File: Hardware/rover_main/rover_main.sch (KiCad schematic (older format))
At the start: 32 parts, among them J1 BATT, J10 Analog, J2 BME280, J3 CSS811, J4 DRIVERS, J5 GY-87, J6 PROG, J7 FTDI, J8 Digital, J9 i2c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

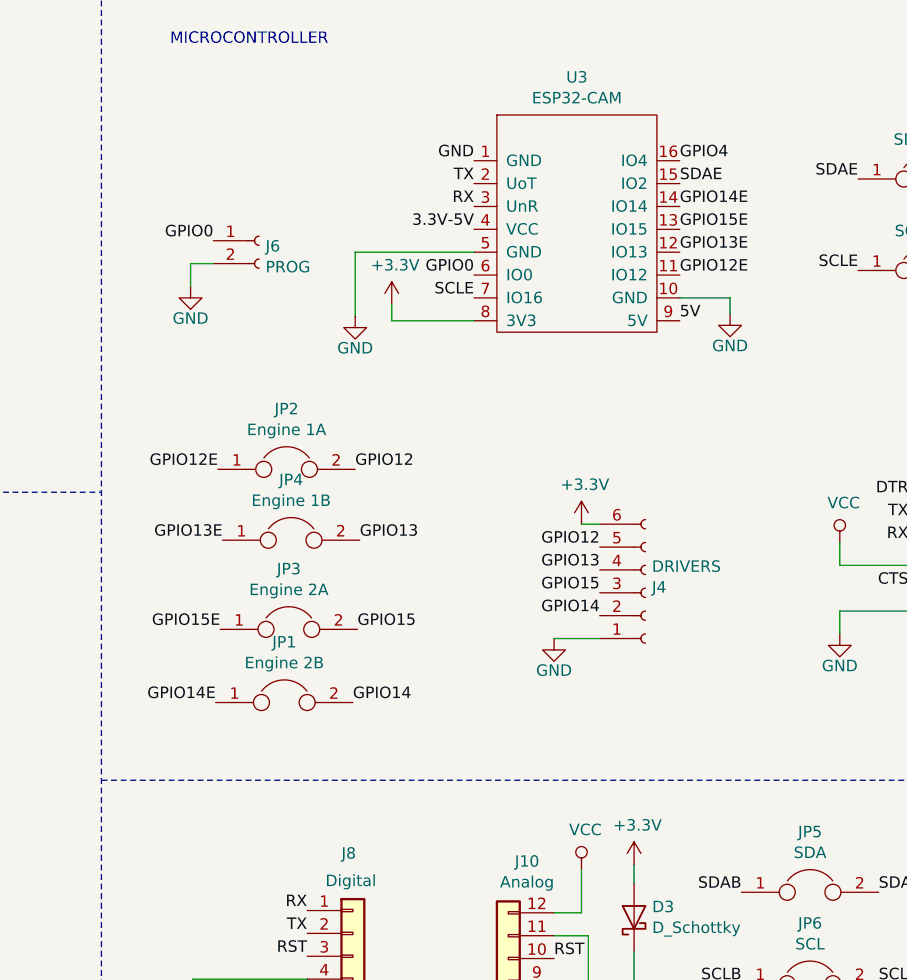
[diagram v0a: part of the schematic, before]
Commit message: Add SDA to jumper
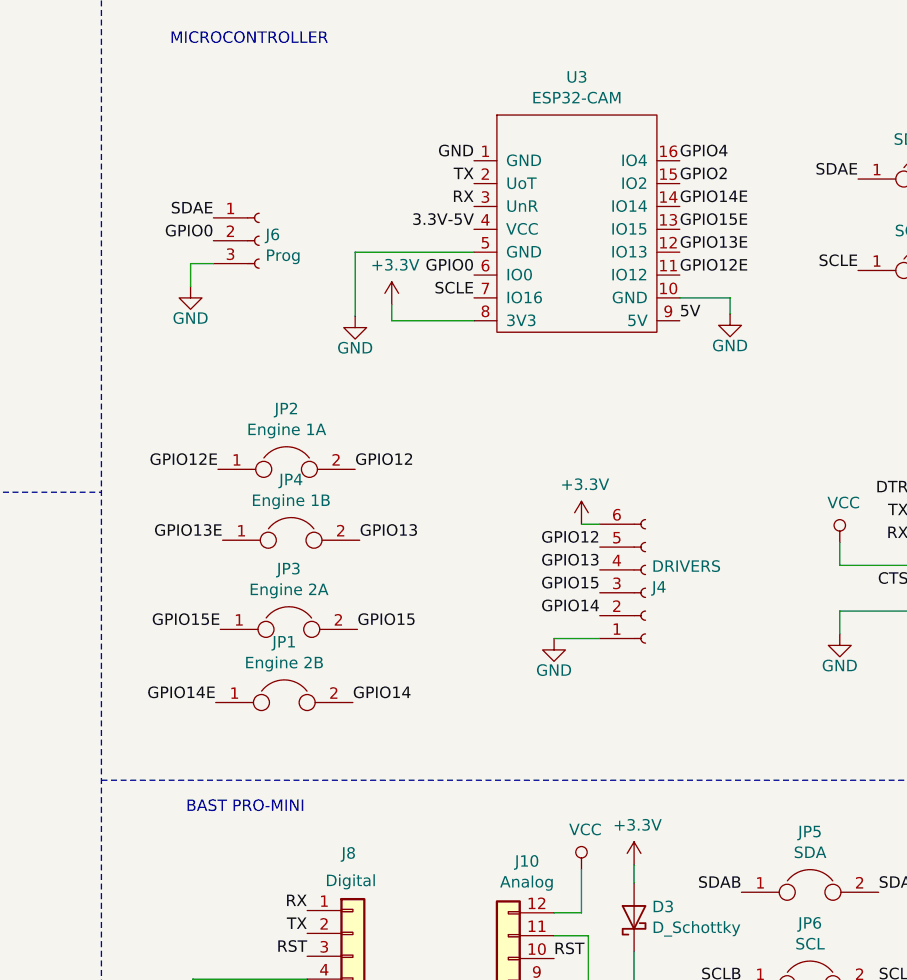
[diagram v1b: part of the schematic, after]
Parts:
- removed J6: PROG, Connector_PinSocket_2.54mm:PinSocket_1x02_P2.54mm_Vertical, symbol Connector:Conn_01x02_Female
- added J6: Prog, Connector_PinHeader_2.54mm:PinHeader_1x03_P2.54mm_Vertical, symbol Connector:Conn_01x03_Female
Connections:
- net GND: now also J6.3 (Pin_3)
- net GPIO0: now also J6.2 (Pin_2)
- net SDAE: now also J6.1 (Pin_1); no longer U3.15 (IO2)
- new net GPIO2: U3.15 (IO2)
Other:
- note added: "BAST PRO-MINI\n"
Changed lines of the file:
@@
 Text Label 10310 1280 2    50   ~ 0
 SDAE
-Text Label 9530 1300 0    50   ~ 0
+Text Label 7490 1450 2    50   ~ 0
 SDAE
 $Comp
@@
 9
 $Comp
-L Connector:Conn_01x02_Female J6
-U 1 1 5D5E84D2
-P 7690 1550
-F 0 "J6" H 7718 1526 50  0000 L CNN
-F 1 "PROG" H 7718 1435 50  0000 L CNN
-F 2 "Connector_PinSocket_2.54mm:PinSocket_1x02_P2.54mm_Vertical" H 7690 1550 50  0001 C CNN
-F 3 "~" H 7690 1550 50  0001 C CNN
-	1    7690 1550
-	1    0    0    -1
-$EndComp
-$Comp
 L Connector:Conn_01x06_Female J2
 U 1 1 5D49D204
@@
 Wire Wire Line
 	9330 4660 9330 4790
+$Comp
+L Connector:Conn_01x03_Female J6
+U 1 1 5D4B08DF
+P 7690 1550
+F 0 "J6" H 7718 1576 50  0000 L CNN
+F 1 "Prog" H 7718 1485 50  0000 L CNN
+F 2 "Connector_PinHeader_2.54mm:PinHeader_1x03_P2.54mm_Vertical" H 7690 1550 50  0001 C CNN
+F 3 "~" H 7690 1550 50  0001 C CNN
+	1    7690 1550
+	1    0    0    -1
+$EndComp
+Text Label 9530 1300 0    50   ~ 0
+GPIO2
+Text Notes 7370 4060 0    50   ~ 0
+BAST PRO-MINI\n
 $EndSCHEMATC

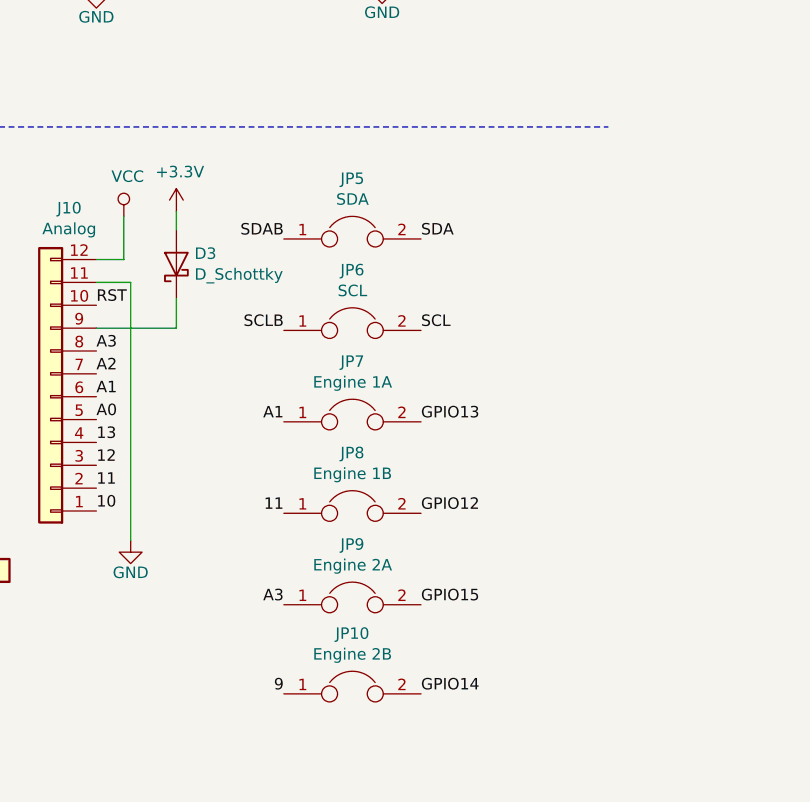
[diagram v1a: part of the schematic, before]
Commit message: change jumper open in sch
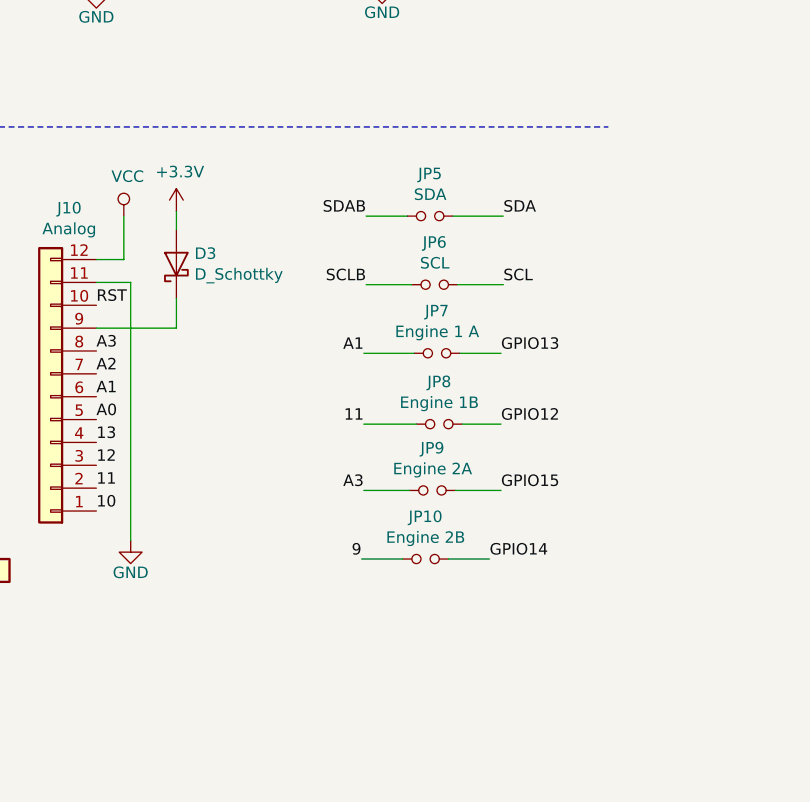
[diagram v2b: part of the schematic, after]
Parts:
- removed JP10: Engine 2B, Jumper:SolderJumper-2_P1.3mm_Open_RoundedPad1.0x1.5mm, symbol Device:Jumper
- removed JP5: SDA, Jumper:SolderJumper-2_P1.3mm_Open_RoundedPad1.0x1.5mm, symbol Device:Jumper
- removed JP6: SCL, Jumper:SolderJumper-2_P1.3mm_Open_RoundedPad1.0x1.5mm, symbol Device:Jumper
- removed JP7: Engine 1A, Jumper:SolderJumper-2_P1.3mm_Open_RoundedPad1.0x1.5mm, symbol Device:Jumper
- removed JP8: Engine 1B, Jumper:SolderJumper-2_P1.3mm_Open_RoundedPad1.0x1.5mm, symbol Device:Jumper
- removed JP9: Engine 2A, Jumper:SolderJumper-2_P1.3mm_Open_RoundedPad1.0x1.5mm, symbol Device:Jumper
- added JP10: Engine 2B, Jumper:SolderJumper-2_P1.3mm_Open_RoundedPad1.0x1.5mm, symbol Device:Jumper_NO_Small
- added JP5: SDA, Jumper:SolderJumper-2_P1.3mm_Open_RoundedPad1.0x1.5mm, symbol Device:Jumper_NO_Small
- added JP6: SCL, Jumper:SolderJumper-2_P1.3mm_Open_RoundedPad1.0x1.5mm, symbol Device:Jumper_NO_Small
- added JP7: Engine 1 A, Jumper:SolderJumper-2_P1.3mm_Open_RoundedPad1.0x1.5mm, symbol Device:Jumper_NO_Small
- added JP8: Engine 1B, Jumper:SolderJumper-2_P1.3mm_Open_RoundedPad1.0x1.5mm, symbol Device:Jumper_NO_Small
- added JP9: Engine 2A, Jumper:SolderJumper-2_P1.3mm_Open_RoundedPad1.0x1.5mm, symbol Device:Jumper_NO_Small
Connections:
- net 11: now also JP8.1
- net 9: now also JP10.1
- net A1: now also JP7.1
- net A3: now also JP9.1
- net GPIO12: now also JP8.2
- net GPIO13: now also JP7.2
- net GPIO14: now also JP10.2
- net GPIO15: now also JP9.2
- net SCL: now also JP6.2
- net SCLB: now also JP6.1
- net SDA: now also JP5.2
- net SDAB: now also JP5.1
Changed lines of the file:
@@
 	0    -1   -1   0
 $EndComp
-$Comp
-L Device:Jumper JP5
-U 1 1 5D4C2B76
-P 10100 4400
-F 0 "JP5" H 10100 4664 50  0000 C CNN
-F 1 "SDA" H 10100 4573 50  0000 C CNN
-F 2 "Jumper:SolderJumper-2_P1.3mm_Open_RoundedPad1.0x1.5mm" H 10100 4400 50  0001 C CNN
-F 3 "~" H 10100 4400 50  0001 C CNN
-	1    10100 4400
-	1    0    0    -1
-$EndComp
-$Comp
-L Device:Jumper JP6
-U 1 1 5D4C33A6
-P 10100 4800
-F 0 "JP6" H 10100 5064 50  0000 C CNN
-F 1 "SCL" H 10100 4973 50  0000 C CNN
-F 2 "Jumper:SolderJumper-2_P1.3mm_Open_RoundedPad1.0x1.5mm" H 10100 4800 50  0001 C CNN
-F 3 "~" H 10100 4800 50  0001 C CNN
-	1    10100 4800
-	1    0    0    -1
-$EndComp
-Text Label 10400 4800 0    50   ~ 0
+Text Label 10760 4600 0    50   ~ 0
 SCL
-Text Label 10400 4400 0    50   ~ 0
+Text Label 10760 4300 0    50   ~ 0
 SDA
-Text Label 9800 4400 2    50   ~ 0
+Text Label 10160 4300 2    50   ~ 0
 SDAB
 Text Label 8450 6050 3    50   ~ 0
 SDAB
-Text Label 9800 4800 2    50   ~ 0
+Text Label 10160 4600 2    50   ~ 0
 SCLB
 Text Label 8550 6050 3    50   ~ 0
 SCLB
-$Comp
-L Device:Jumper JP10
-U 1 1 5D4C8EC9
-P 10100 6390
-F 0 "JP10" H 10100 6654 50  0000 C CNN
-F 1 "Engine 2B" H 10100 6563 50  0000 C CNN
-F 2 "Jumper:SolderJumper-2_P1.3mm_Open_RoundedPad1.0x1.5mm" H 10100 6390 50  0001 C CNN
-F 3 "~" H 10100 6390 50  0001 C CNN
-	1    10100 6390
-	1    0    0    -1
-$EndComp
-$Comp
-L Device:Jumper JP9
-U 1 1 5D4C93D4
-P 10100 6000
-F 0 "JP9" H 10100 6264 50  0000 C CNN
-F 1 "Engine 2A" H 10100 6173 50  0000 C CNN
-F 2 "Jumper:SolderJumper-2_P1.3mm_Open_RoundedPad1.0x1.5mm" H 10100 6000 50  0001 C CNN
-F 3 "~" H 10100 6000 50  0001 C CNN
-	1    10100 6000
-	1    0    0    -1
-$EndComp
-$Comp
-L Device:Jumper JP8
-U 1 1 5D4C97D6
-P 10100 5600
-F 0 "JP8" H 10100 5864 50  0000 C CNN
-F 1 "Engine 1B" H 10100 5773 50  0000 C CNN
-F 2 "Jumper:SolderJumper-2_P1.3mm_Open_RoundedPad1.0x1.5mm" H 10100 5600 50  0001 C CNN
-F 3 "~" H 10100 5600 50  0001 C CNN
-	1    10100 5600
-	1    0    0    -1
-$EndComp
-Text Label 9800 6000 2    50   ~ 0
+Text Label 10150 5500 2    50   ~ 0
 A3
-Text Label 10400 5600 0    50   ~ 0
+Text Label 10750 5210 0    50   ~ 0
 GPIO12
-$Comp
-L Device:Jumper JP7
-U 1 1 5D4C892D
-P 10100 5200
-F 0 "JP7" H 10100 5464 50  0000 C CNN
-F 1 "Engine 1A" H 10100 5373 50  0000 C CNN
-F 2 "Jumper:SolderJumper-2_P1.3mm_Open_RoundedPad1.0x1.5mm" H 10100 5200 50  0001 C CNN
-F 3 "~" H 10100 5200 50  0001 C CNN
-	1    10100 5200
-	1    0    0    -1
-$EndComp
-Text Label 10400 5200 0    50   ~ 0
+Text Label 10750 4900 0    50   ~ 0
 GPIO13
-Text Label 10400 6000 0    50   ~ 0
+Text Label 10750 5500 0    50   ~ 0
 GPIO15
-Text Label 10400 6390 0    50   ~ 0
+Text Label 10700 5800 0    50   ~ 0
 GPIO14
 $Comp
@@
 Text Label 5290 6000 2    50   ~ 0
 VCC-IN
-Text Label 9800 5600 2    50   ~ 0
+Text Label 10150 5210 2    50   ~ 0
 11
-Text Label 9800 5200 2    50   ~ 0
+Text Label 10150 4900 2    50   ~ 0
 A1
-Text Label 9800 6390 2    50   ~ 0
+Text Label 10140 5800 2    50   ~ 0
 9
 $Comp
@@
 Text Notes 7370 4060 0    50   ~ 0
 BAST PRO-MINI\n
+$Comp
+L Device:Jumper_NO_Small JP5
+U 1 1 5D4C5CB0
+P 10440 4300
+F 0 "JP5" H 10440 4485 50  0000 C CNN
+F 1 "SDA" H 10440 4394 50  0000 C CNN
+F 2 "Jumper:SolderJumper-2_P1.3mm_Open_RoundedPad1.0x1.5mm" H 10440 4300 50  0001 C CNN
+F 3 "~" H 10440 4300 50  0001 C CNN
+	1    10440 4300
+	1    0    0    -1
+$EndComp
+$Comp
+L Device:Jumper_NO_Small JP6
+U 1 1 5D4C667E
+P 10460 4600
+F 0 "JP6" H 10460 4785 50  0000 C CNN
+F 1 "SCL" H 10460 4694 50  0000 C CNN
+F 2 "Jumper:SolderJumper-2_P1.3mm_Open_RoundedPad1.0x1.5mm" H 10460 4600 50  0001 C CNN
+F 3 "~" H 10460 4600 50  0001 C CNN
+	1    10460 4600
+	1    0    0    -1
+$EndComp
+Wire Wire Line
+	10540 4300 10760 4300
+Wire Wire Line
+	10340 4300 10160 4300
+Wire Wire Line
+	10760 4600 10560 4600
+Wire Wire Line
+	10160 4600 10360 4600
+$Comp
+L Device:Jumper_NO_Small JP7
+U 1 1 5D4CD611
+P 10470 4900
+F 0 "JP7" H 10470 5085 50  0000 C CNN
+F 1 "Engine 1 A" H 10470 4994 50  0000 C CNN
+F 2 "Jumper:SolderJumper-2_P1.3mm_Open_RoundedPad1.0x1.5mm" H 10470 4900 50  0001 C CNN
+F 3 "~" H 10470 4900 50  0001 C CNN
+	1    10470 4900
+	1    0    0    -1
+$EndComp
+Wire Wire Line
+	10570 4900 10750 4900
+Wire Wire Line
+	10370 4900 10150 4900
+$Comp
+L Device:Jumper_NO_Small JP8
+U 1 1 5D4D2033
+P 10480 5210
+F 0 "JP8" H 10480 5395 50  0000 C CNN
+F 1 "Engine 1B" H 10480 5304 50  0000 C CNN
+F 2 "Jumper:SolderJumper-2_P1.3mm_Open_RoundedPad1.0x1.5mm" H 10480 5210 50  0001 C CNN
+F 3 "~" H 10480 5210 50  0001 C CNN
+	1    10480 5210
+	1    0    0    -1
+$EndComp
+Wire Wire Line
+	10580 5210 10750 5210
+Wire Wire Line
+	10380 5210 10150 5210
+$Comp
+L Device:Jumper_NO_Small JP9
+U 1 1 5D4D5761
+P 10450 5500
+F 0 "JP9" H 10450 5685 50  0000 C CNN
+F 1 "Engine 2A" H 10450 5594 50  0000 C CNN
+F 2 "Jumper:SolderJumper-2_P1.3mm_Open_RoundedPad1.0x1.5mm" H 10450 5500 50  0001 C CNN
+F 3 "~" H 10450 5500 50  0001 C CNN
+	1    10450 5500
+	1    0    0    -1
+$EndComp
+Wire Wire Line
+	10550 5500 10750 5500
+Wire Wire Line
+	10150 5500 10350 5500
+$Comp
+L Device:Jumper_NO_Small JP10
+U 1 1 5D4DA54D
+P 10420 5800
+F 0 "JP10" H 10420 5985 50  0000 C CNN
+F 1 "Engine 2B" H 10420 5894 50  0000 C CNN
+F 2 "Jumper:SolderJumper-2_P1.3mm_Open_RoundedPad1.0x1.5mm" H 10420 5800 50  0001 C CNN
+F 3 "~" H 10420 5800 50  0001 C CNN
+	1    10420 5800
+	1    0    0    -1
+$EndComp
+Wire Wire Line
+	10520 5800 10700 5800
+Wire Wire Line
+	10320 5800 10140 5800
 $EndSCHEMATC

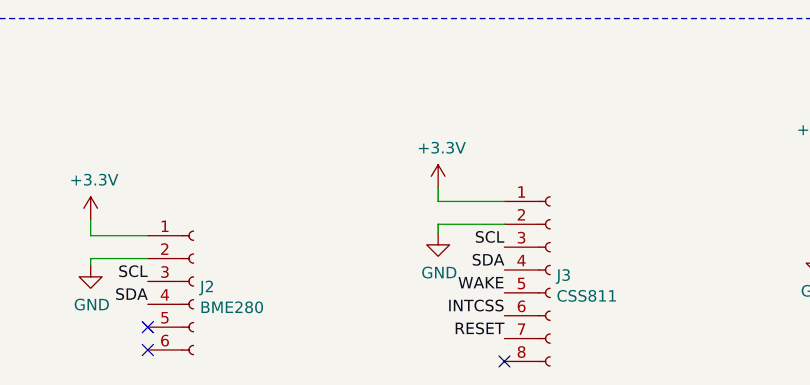
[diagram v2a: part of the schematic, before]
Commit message: fix conections CCS811
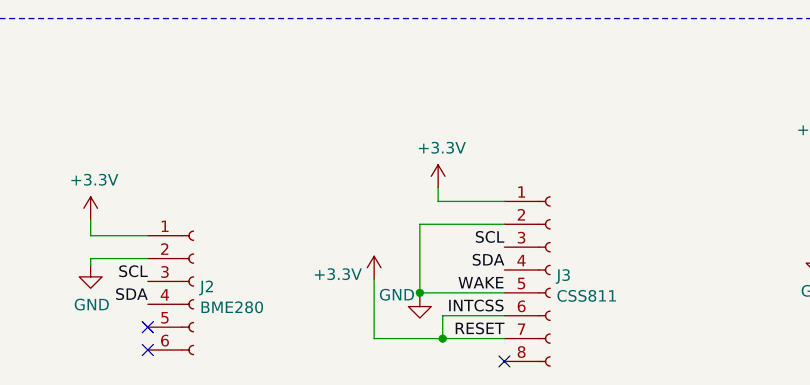
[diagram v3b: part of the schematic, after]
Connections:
- net INTCSS is gone; now on net +3V3: J3.6 (Pin_6)
- net RESET is gone; now on net +3V3: J3.7 (Pin_7)
- net WAKE is gone; now on net GND: J3.5 (Pin_5)
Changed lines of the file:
@@
 	1760 6310 2010 6310
-$Comp
-L power:GND #PWR09
-U 1 1 5D24666B
-P 3280 6200
-F 0 "#PWR09" H 3280 5950 50  0001 C CNN
-F 1 "GND" H 3285 6027 50  0000 C CNN
-F 2 "" H 3280 6200 50  0001 C CNN
-F 3 "" H 3280 6200 50  0001 C CNN
-	1    3280 6200
-	1    0    0    -1
-$EndComp
 $Comp
 L power:+3.3V #PWR08
@@
 Wire Wire Line
 	3280 6060 3570 6060
-Wire Wire Line
-	3280 6200 3280 6160
-Wire Wire Line
-	3280 6160 3570 6160
 $Comp
 L rover_main-rescue:MCP732831CHARGER-electroniccats U2
@@
 Wire Wire Line
 	10320 5800 10140 5800
+$Comp
+L power:+3.3V #PWR?
+U 1 1 5D54B969
+P 3000 6400
+F 0 "#PWR?" H 3000 6250 50  0001 C CNN
+F 1 "+3.3V" H 2840 6420 50  0000 C CNN
+F 2 "" H 3000 6400 50  0001 C CNN
+F 3 "" H 3000 6400 50  0001 C CNN
+	1    3000 6400
+	1    0    0    -1
+$EndComp
+$Comp
+L power:GND #PWR?
+U 1 1 5D544C06
+P 3200 6470
+F 0 "#PWR?" H 3200 6220 50  0001 C CNN
+F 1 "GND" H 3100 6470 50  0000 C CNN
+F 2 "" H 3200 6470 50  0001 C CNN
+F 3 "" H 3200 6470 50  0001 C CNN
+	1    3200 6470
+	1    0    0    -1
+$EndComp
+Wire Wire Line
+	3570 6460 3200 6460
+Wire Wire Line
+	3200 6460 3200 6470
+Wire Wire Line
+	3570 6160 3200 6160
+Wire Wire Line
+	3200 6160 3200 6460
+Connection ~ 3200 6460
+Wire Wire Line
+	3570 6560 3300 6560
+Wire Wire Line
+	3300 6560 3300 6660
+Wire Wire Line
+	3300 6660 3570 6660
+Wire Wire Line
+	3300 6660 3000 6660
+Connection ~ 3300 6660
+Wire Wire Line
+	3000 6660 3000 6400
 $EndSCHEMATC
